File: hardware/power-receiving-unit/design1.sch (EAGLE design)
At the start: 93 parts, among them IC12 NRF52832, IC3 TPS54308DDCR, IC4 MCP6486T-E/OT, Q1 BSS138, Q2 SI3481DV, Y1 32MHz, Y2 32.768kHz

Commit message: Update SW PRU & HW PRU + PTU
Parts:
- removed IC12: NRF52832, SparkFun-RF:NRF52832
- added IC2: (no value), SparkFun-RF:NRF52832-EXTENDED
- C7: value 10u -> DNP
- R15: value 100k -> 15k
- R3, R4: value 1k -> 1k2
- R7: value R025 -> R020
- R9: value 4k7 -> 10k
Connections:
- removed net NC: IC12.NC
- net !RESET!: now also IC2.P0.21/RESET; no longer IC12.P0.21/RESET
- net ANT: now also IC2.ANT; no longer IC12.ANT
- net DCC: now also IC2.DCC; no longer IC12.DCC
- net DEC4: now also IC2.DEC4; no longer IC12.DEC4
- net DEC5: now also IC2.DEC1; no longer IC12.DEC1
- net DEC6: now also IC2.DEC2; no longer IC12.DEC2
- net DEC8: now also IC2.DEC3; no longer IC12.DEC3
- net EN_SENS: now also IC2.P0.20; no longer IC12.P0.20
- net GND: now also IC2.VSS; no longer IC12.VSS
- net I2C_SCL: now also IC2.P0.27; no longer IC12.P0.27
- net I2C_SDA: now also IC2.P0.26; no longer IC12.P0.26
- net LED: now also IC2.P0.15; no longer IC12.P0.15
- net MISO: now also IC2.P0.29/AIN5; no longer IC12.P0.29/AIN5
- net MOSI: now also IC2.P0.30/AIN6; no longer IC12.P0.30/AIN6
- net N$50: now also IC2.P0.25; no longer IC12.P0.25
- net P00: now also IC2.P0.00/XL1; no longer IC12.P0.00/XL1
- net P01: now also IC2.P0.01/XL2; no longer IC12.P0.01/XL2
- net P02: now also IC2.P0.02/AIN0; no longer IC12.P0.02/AIN0
- net P03: now also IC2.P0.03/AIN1; no longer IC12.P0.03/AIN1
- net P04: now also IC2.P0.04/AIN2; no longer IC12.P0.04/AIN2
- net P05: now also IC2.P0.05/AIN3; no longer IC12.P0.05/AIN3
- net P06: now also IC2.P0.06; no longer IC12.P0.06
- net P07: now also IC2.P0.07; no longer IC12.P0.07
- net P08: now also IC2.P0.08; no longer IC12.P0.08
- net P09: now also IC2.P0.09/NFC1; no longer IC12.P0.09/NFC1
- net P10: now also IC2.P0.10/NFC2; no longer IC12.P0.10/NFC2
- net P11: now also IC2.P0.11; no longer IC12.P0.11
- net P12: now also IC2.P0.12; no longer IC12.P0.12
- net P13: now also IC2.P0.13; no longer IC12.P0.13
- net P14: now also IC2.P0.14; no longer IC12.P0.14
- net P16: now also IC2.P0.16; no longer IC12.P0.16
- net P17: now also IC2.P0.17; no longer IC12.P0.17
- net P19: now also IC2.P0.19; no longer IC12.P0.19
- net P22: now also IC2.P0.22; no longer IC12.P0.22
- net P23: now also IC2.P0.23; no longer IC12.P0.23
- net P24: now also IC2.P0.24; no longer IC12.P0.24
- net P28: now also IC2.P0.28/AIN4; no longer IC12.P0.28/AIN4
- net SCK: now also IC2.P0.31/AIN7; no longer IC12.P0.31/AIN7
- net SWDCLK: now also IC2.SWDCLK; no longer IC12.SWDCLK
- net SWDIO: now also IC2.SWDIO; no longer IC12.SWDIO
- net SWO/TDO: now also IC2.P0.18; no longer IC12.P0.18
- net VDD_BLE: now also IC2.VDD; no longer IC12.VDD
- net XC1: now also IC2.XC1(32MHZ); no longer IC12.XC1(32MHZ)
- net XC2: now also IC2.XC2(32MHZ); no longer IC12.XC2(32MHZ)
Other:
- note added: "CHANGE TO 68K"
- note added: "Change to pull up !!!"
- note added: "DNP"
- note added: "Footprint updated (14/08/23)"
- note added: "MIC94081YFT-TR VOLTAGE RANGE (1.7 - 5.5V)"
- note added: "SOLDER"
- note added: "ToDo: ADD Load Switch + Voltage Div to read output voltage"
- note added: "https://infocenter.nordicsemi.com/index.jsp?topic=%2Fug_nrf52832_pdk%2FUG%2Fnrf52_PDK%2Fhw_debug_out.html"

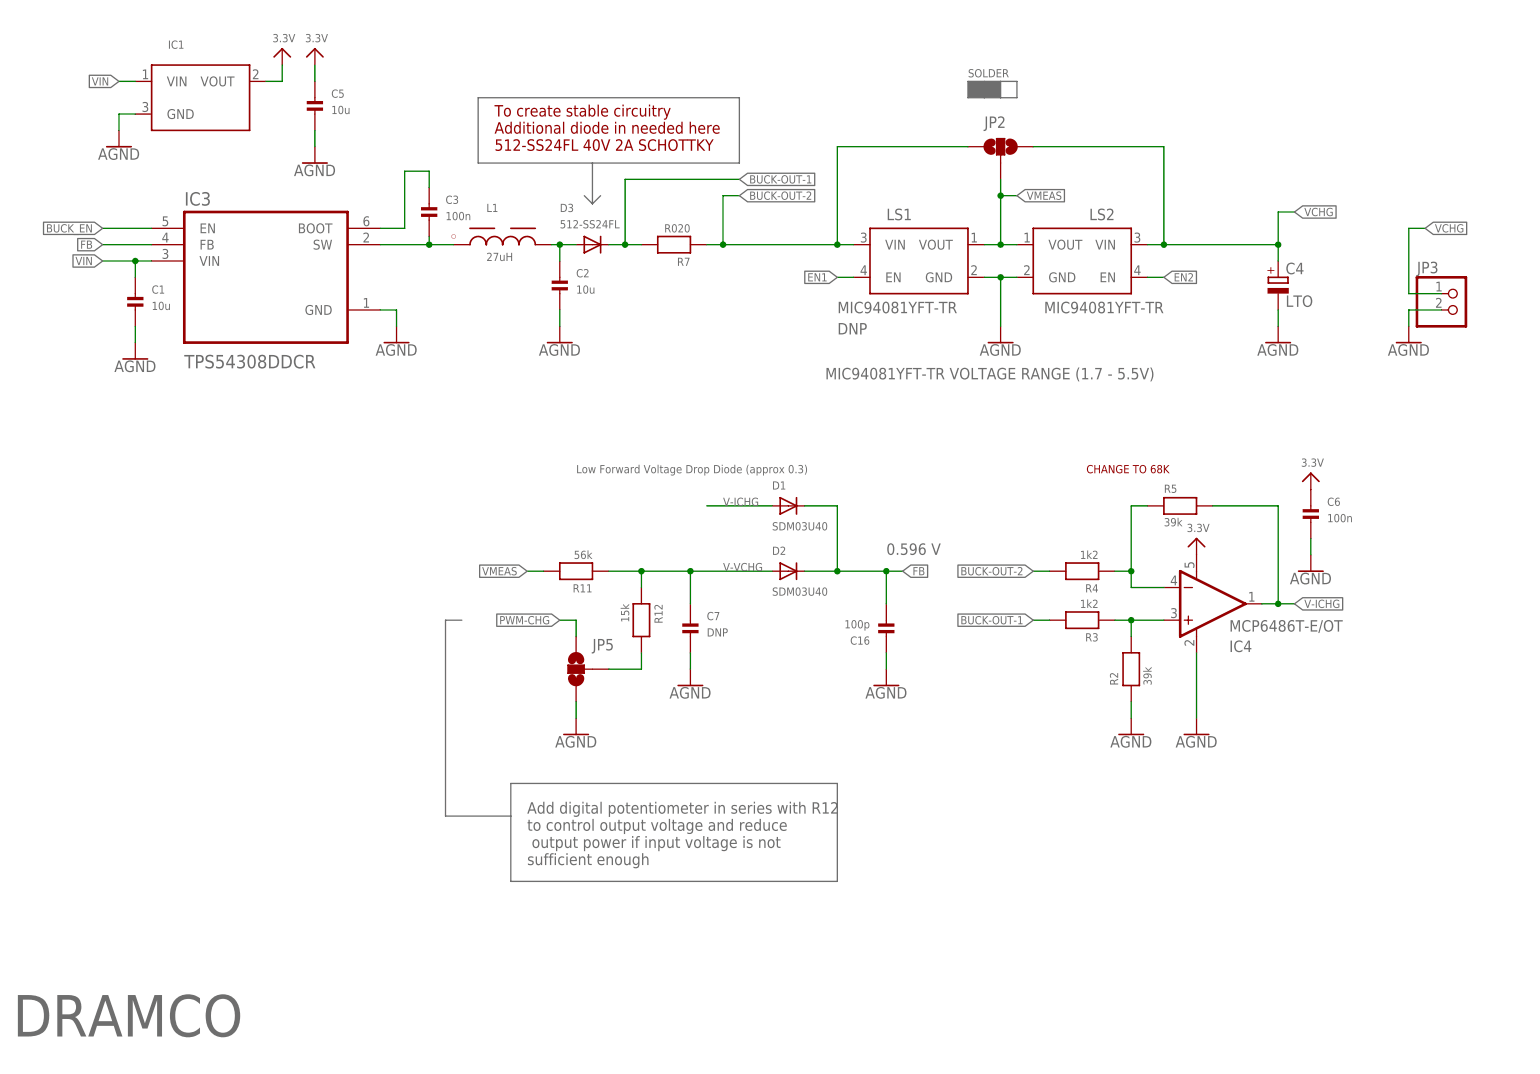
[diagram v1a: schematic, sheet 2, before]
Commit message: Update PRU HW + firmware (send pru info via BLE adv)
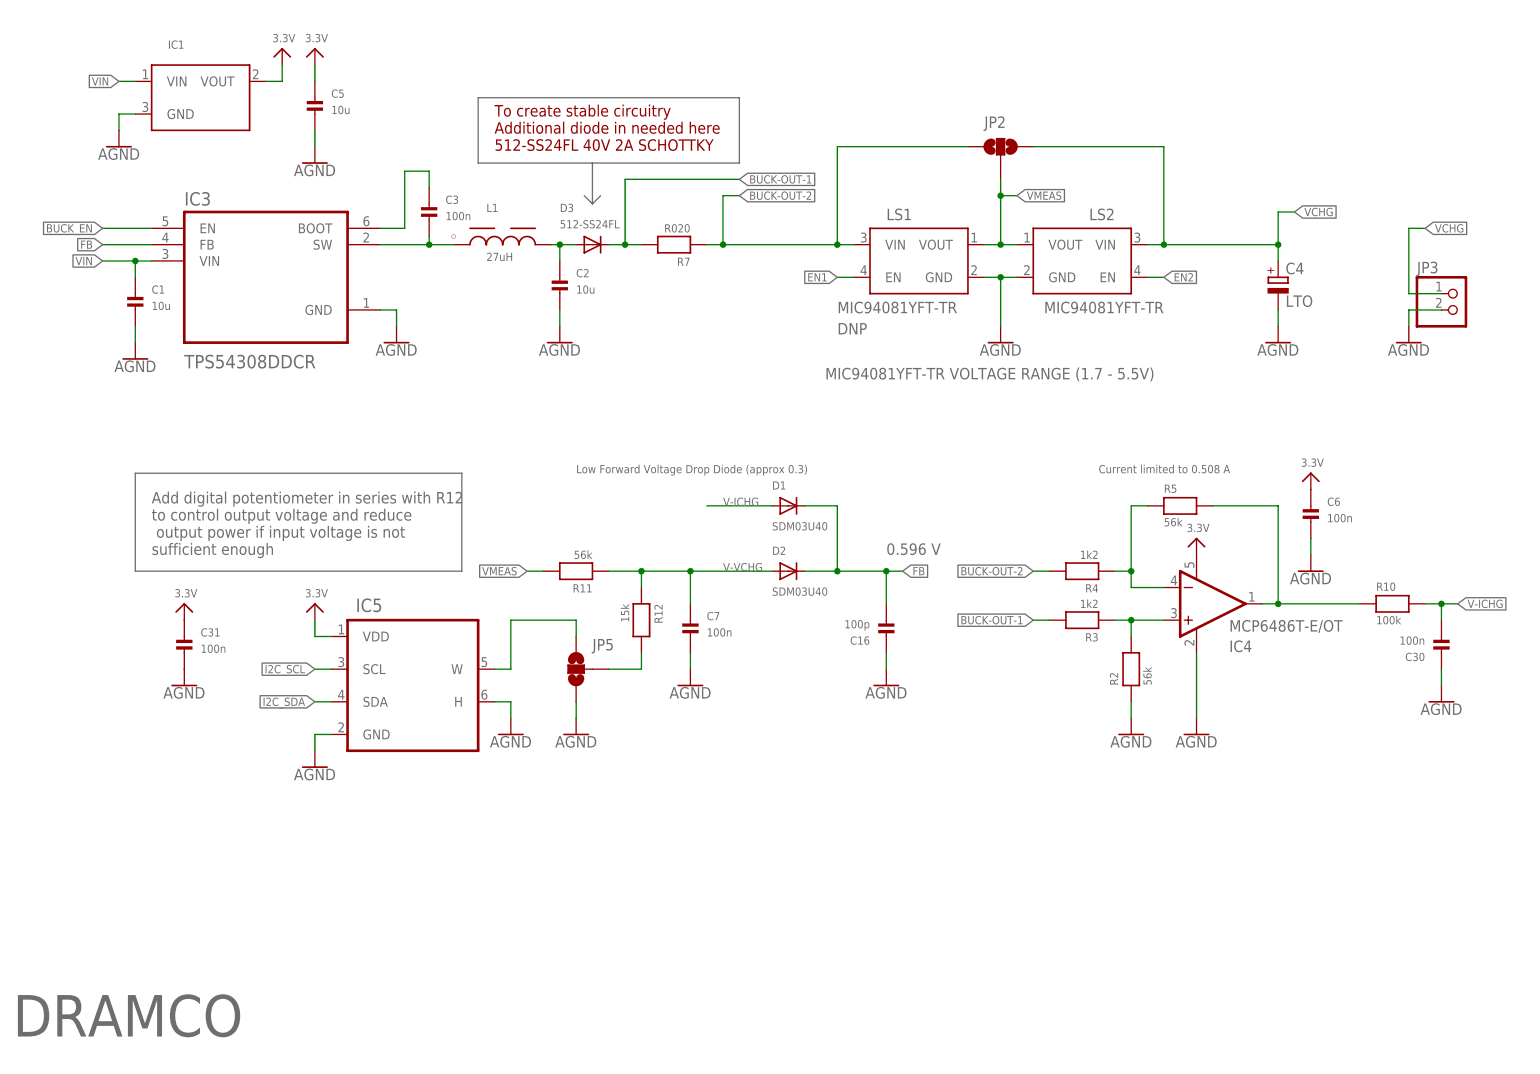
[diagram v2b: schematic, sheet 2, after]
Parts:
- added C30, C31: 100n, microbuilder:CAP_CERAMIC0603
- added C32: 100n, microbuilder:CAP_CERAMIC0402
- added IC5: (no value), TPL0401A-10DCKR:TPL0401A-10DCKR
- added L7: 742792692, PowerMagnetics (rev18e):WE-CBF_0603_742792692_WB_HS
- added R10: 100k, microbuilder:RESISTOR0603
- C7: value DNP -> 100n
- R2, R5: value 39k -> 56k
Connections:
- new net N$7: JP4.2, L7.1
- net 3.3V: now also C31.P$1, IC5.VDD
- net AGND: now also C30.P$1, C31.P$2, IC5.GND, IC5.H
- net GND: now also C32.P$2
- net I2C_SCL: now also IC5.SCL
- net I2C_SDA: now also IC5.SDA
- net P19: now also C32.P$1
- net PWM-CHG: now also IC5.W
- net V-ICHG: now also C30.P$2, R10.1, R10.2
- net V-VCHG: no longer JP13.2
- net VDD_BLE: now also JP13.2, L7.2; no longer JP4.2
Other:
- note added: "Current limited to 0.508 A"
- note removed: "CHANGE TO 68K"
- note removed: "SOLDER"

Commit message: Update hardware PTU
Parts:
- removed LS1, LS2: MIC94081YFT-TR, MIC94081YFT-TR:MIC94081YFT-TR
- added JP15: JUMPER-SMT_2_NO_NO-SILK, SparkFun-Jumpers:JUMPER-SMT_2_NO_NO-SILK
- added Q3: PMDPB55XP, PMDPB55XP:PMDPB55XP
- added Q4, Q5: DMG1012T, microbuilder:DMG1012T
- added R13, R17: 100k, microbuilder:RESISTOR0402
- added R18, R19: 4k7, microbuilder:RESISTOR0402
- C23: value DNP -> 0.8p
- C31: device microbuilder:CAP_CERAMIC0603 -> microbuilder:CAP_CERAMIC0402
- renumbered UART_INTERFACE to UART
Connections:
- removed net N$13: C2.P$1, D3.A, L1.2
- removed net PWM-CHG: IC5.W, JP10.2, JP5.3
- new net DIGI-POT: IC5.W, JP5.3
- new net I2C_PULLUP: JP10.2, R18.1, R19.1
- new net N$1: JP2.2, Q3.D1, Q3.D2
- new net N$17: Q3.G1, Q4.D, R17.2
- new net N$18: Q3.G2, Q5.D, R13.2
- new net OPAMP-OUT: IC4.OUT, R10.1, R5.2
- net AGND: now also Q4.S, Q5.S; no longer LS1.GND, LS2.GND
- net BUCK-OUT-1: now also C2.P$1, L1.2; no longer D3.C
- net BUCK-OUT-2: now also D3.A; no longer JP2.1, LS1.VIN
- net EN1: now also Q4.G; no longer LS1.EN
- net EN2: now also Q5.G; no longer LS2.EN
- net I2C_SCL: now also R19.2
- net I2C_SDA: now also R18.2
- net V-ICHG: no longer IC4.OUT, R10.1, R5.2
- net VCHG: now also Q3.S2, R13.1; no longer LS2.VIN
- net VDD_BLE: now also JP15.1
- net VDD_SENS: now also JP15.2
- net VMEAS: now also D3.C, JP2.1, Q3.S1, R17.1; no longer JP2.2, LS1.VOUT, LS2.VOUT
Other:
- note removed: "Change to pull up !!!"
- note removed: "DNP"
- note removed: "MIC94081YFT-TR VOLTAGE RANGE (1.7 - 5.5V)"
- note removed: "ToDo: ADD Load Switch + Voltage Div to read output voltage"
- moved on the sheet: D3, JP2, R7

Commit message: Update PTU firmware and hardware
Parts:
- added JP17: JUMPER-SMT_2_NO_NO-SILK, SparkFun-Jumpers:JUMPER-SMT_2_NO_NO-SILK
- added LS1: MIC94081YFT-TR, MIC94081YFT-TR:MIC94081YFT-TR
- UART: device microbuilder:HEADER-1X4ROUND -> microbuilder:HEADER-1X5ROUND
- renumbered LS3 to LS2
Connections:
- removed net P22: IC2.P0.22
- new net EN_MDM: IC2.P0.22, LS1.EN
- new net VDD_MDM: JP17.2, LS1.VOUT, UART.1
- net GND: now also LS1.GND
- net P05: now also UART.4; no longer UART.3
- net P06: now also UART.3; no longer UART.2
- net P07: now also UART.5; no longer UART.4
- net P08: now also UART.2; no longer UART.1
- net VDD_BLE: now also JP17.1, LS1.VIN

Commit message: Update firmware - hardware all
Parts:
- C23: value 0.8p -> 1.2p
- D1, D2: value SDM03U40 -> RB751S40T1G
- IC1: value (none) -> AP7381-33SA-7
- IC5: value (none) -> TPL0401A-10DCKR
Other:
- note added: "MAX 40V input"
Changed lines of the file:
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@@
 <part name="C1" library="microbuilder" deviceset="CAP_CERAMIC" device="0603" value="10u"/>
 <part name="C2" library="microbuilder" deviceset="CAP_CERAMIC" device="0603" value="10u"/>
-<part name="D1" library="microbuilder" deviceset="DIODE" device="SOD-523" value="SDM03U40"/>
-<part name="D2" library="microbuilder" deviceset="DIODE" device="SOD-523" value="SDM03U40"/>
+<part name="D1" library="microbuilder" deviceset="DIODE" device="SOD-523" value="RB751S40T1G"/>
+<part name="D2" library="microbuilder" deviceset="DIODE" device="SOD-523" value="RB751S40T1G"/>
 <part name="R11" library="microbuilder" deviceset="RESISTOR" device="0603" value="56k"/>
 <part name="R12" library="microbuilder" deviceset="RESISTOR" device="0603" value="15k"/>
@@
 <part name="R4" library="microbuilder" deviceset="RESISTOR" device="0603" value="1k2"/>
 <part name="R5" library="microbuilder" deviceset="RESISTOR" device="0603" value="56k"/>
-<part name="IC1" library="microbuilder" deviceset="VREG_SOT23" device=""/>
+<part name="IC1" library="microbuilder" deviceset="VREG_SOT23" device="" value="AP7381-33SA-7"/>
 <part name="U$1" library="microbuilder" deviceset="3.3V" device=""/>
 <part name="C5" library="microbuilder" deviceset="CAP_CERAMIC" device="0603" value="10u"/>
@@
 <part name="C21" library="microbuilder" deviceset="CAP_CERAMIC" device="0402" value="100n"/>
 <part name="C22" library="microbuilder" deviceset="CAP_CERAMIC" device="0402" value="100n"/>
-<part name="C23" library="microbuilder" deviceset="CAP_CERAMIC" device="0402" value="0.8p"/>
+<part name="C23" library="microbuilder" deviceset="CAP_CERAMIC" device="0402" value="1.2p"/>
 <part name="C24" library="microbuilder" deviceset="CAP_CERAMIC" device="0402" value="0.8p"/>
 <part name="C25" library="microbuilder" deviceset="CAP_CERAMIC" device="0402" value="12p"/>
@@
 <part name="C30" library="microbuilder" deviceset="CAP_CERAMIC" device="0603" value="100n"/>
 <part name="U$24" library="SparkFun-PowerSymbols" deviceset="AGND" device=""/>
-<part name="IC5" library="TPL0401A-10DCKR" deviceset="TPL0401A-10DCKR" device=""/>
+<part name="IC5" library="TPL0401A-10DCKR" deviceset="TPL0401A-10DCKR" device="" value="TPL0401A-10DCKR"/>
 <part name="U$25" library="SparkFun-PowerSymbols" deviceset="AGND" device=""/>
 <part name="U$26" library="SparkFun-PowerSymbols" deviceset="AGND" device=""/>
@@
 <text x="6.35" y="6.35" size="6.4516" layer="95">DRAMCO</text>
 <text x="175.26" y="93.98" size="1.27" layer="95">Current limited to 0.508 A</text>
+<text x="10.16" y="160.02" size="1.778" layer="95">MAX 40V input</text>
 </plain>
 <instances>
